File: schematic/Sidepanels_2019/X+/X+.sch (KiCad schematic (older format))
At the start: 33 parts, among them J1 Conn_01x04, J2 Conn_01x02

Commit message: Flipped and added TrisolX cells
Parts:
- added D16: D_Schottky, CySat footprints:Toshiba_CUS08F30, symbol Device:D_Schottky
- added SC17: Solar_Cell, CySat footprints:TriSelectSolarPanel_Left_Handed, symbol Device:Solar_Cell
- SC10, SC11, SC12, SC13, SC14, SC15, SC16, SC5, SC6, SC7, SC8, SC9: footprint CySat footprints:TriSelectSolarPanel -> CySat footprints:TriSelectSolarPanel_Left_Handed
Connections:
- net VCC: now also D16.1 (K), SC17.1 (+)
- net VSS: now also D16.2 (A), SC17.2 (-)
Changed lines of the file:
@@
 EESchema Schematic File Version 4
+LIBS:X+-cache
 EELAYER 29 0
 EELAYER END
@@
 F 0 "SC10" H 6308 2446 50  0000 L CNN
 F 1 "Solar_Cell" H 6308 2355 50  0000 L CNN
-F 2 "CySat footprints:TriSelectSolarPanel" V 6200 2410 50  0001 C CNN
+F 2 "CySat footprints:TriSelectSolarPanel_Left_Handed" V 6200 2410 50  0001 C CNN
 F 3 "~" V 6200 2410 50  0001 C CNN
 	1    6200 2350
@@
 F 0 "SC9" H 5458 2446 50  0000 L CNN
 F 1 "Solar_Cell" H 5458 2355 50  0000 L CNN
-F 2 "CySat footprints:TriSelectSolarPanel" V 5350 2410 50  0001 C CNN
+F 2 "CySat footprints:TriSelectSolarPanel_Left_Handed" V 5350 2410 50  0001 C CNN
 F 3 "~" V 5350 2410 50  0001 C CNN
 	1    5350 2350
@@
 F 0 "SC12" H 8008 2446 50  0000 L CNN
 F 1 "Solar_Cell" H 8008 2355 50  0000 L CNN
-F 2 "CySat footprints:TriSelectSolarPanel" V 7900 2410 50  0001 C CNN
+F 2 "CySat footprints:TriSelectSolarPanel_Left_Handed" V 7900 2410 50  0001 C CNN
 F 3 "~" V 7900 2410 50  0001 C CNN
 	1    7900 2350
@@
 F 0 "SC13" H 8708 2446 50  0000 L CNN
 F 1 "Solar_Cell" H 8708 2355 50  0000 L CNN
-F 2 "CySat footprints:TriSelectSolarPanel" V 8600 2410 50  0001 C CNN
+F 2 "CySat footprints:TriSelectSolarPanel_Left_Handed" V 8600 2410 50  0001 C CNN
 F 3 "~" V 8600 2410 50  0001 C CNN
 	1    8600 2350
@@
 F 0 "SC16" H 10808 2446 50  0000 L CNN
 F 1 "Solar_Cell" H 10808 2355 50  0000 L CNN
-F 2 "CySat footprints:TriSelectSolarPanel" V 10700 2410 50  0001 C CNN
+F 2 "CySat footprints:TriSelectSolarPanel_Left_Handed" V 10700 2410 50  0001 C CNN
 F 3 "~" V 10700 2410 50  0001 C CNN
 	1    10700 2350
@@
 F 0 "SC6" H 3108 2446 50  0000 L CNN
 F 1 "Solar_Cell" H 3108 2355 50  0000 L CNN
-F 2 "CySat footprints:TriSelectSolarPanel" V 3000 2410 50  0001 C CNN
+F 2 "CySat footprints:TriSelectSolarPanel_Left_Handed" V 3000 2410 50  0001 C CNN
 F 3 "~" V 3000 2410 50  0001 C CNN
 	1    3000 2350
@@
 F 0 "SC5" H 2458 2446 50  0000 L CNN
 F 1 "Solar_Cell" H 2458 2355 50  0000 L CNN
-F 2 "CySat footprints:TriSelectSolarPanel" V 2350 2410 50  0001 C CNN
+F 2 "CySat footprints:TriSelectSolarPanel_Left_Handed" V 2350 2410 50  0001 C CNN
 F 3 "~" V 2350 2410 50  0001 C CNN
 	1    2350 2350
@@
 F 0 "SC7" H 3758 2446 50  0000 L CNN
 F 1 "Solar_Cell" H 3758 2355 50  0000 L CNN
-F 2 "CySat footprints:TriSelectSolarPanel" V 3650 2410 50  0001 C CNN
+F 2 "CySat footprints:TriSelectSolarPanel_Left_Handed" V 3650 2410 50  0001 C CNN
 F 3 "~" V 3650 2410 50  0001 C CNN
 	1    3650 2350
@@
 F 0 "SC8" H 4608 2446 50  0000 L CNN
 F 1 "Solar_Cell" H 4608 2355 50  0000 L CNN
-F 2 "CySat footprints:TriSelectSolarPanel" V 4500 2410 50  0001 C CNN
+F 2 "CySat footprints:TriSelectSolarPanel_Left_Handed" V 4500 2410 50  0001 C CNN
 F 3 "~" V 4500 2410 50  0001 C CNN
 	1    4500 2350
@@
 F 0 "SC11" H 7158 2446 50  0000 L CNN
 F 1 "Solar_Cell" H 7158 2355 50  0000 L CNN
-F 2 "CySat footprints:TriSelectSolarPanel" V 7050 2410 50  0001 C CNN
+F 2 "CySat footprints:TriSelectSolarPanel_Left_Handed" V 7050 2410 50  0001 C CNN
 F 3 "~" V 7050 2410 50  0001 C CNN
 	1    7050 2350
@@
 F 0 "SC15" H 10108 2446 50  0000 L CNN
 F 1 "Solar_Cell" H 10108 2355 50  0000 L CNN
-F 2 "CySat footprints:TriSelectSolarPanel" V 10000 2410 50  0001 C CNN
+F 2 "CySat footprints:TriSelectSolarPanel_Left_Handed" V 10000 2410 50  0001 C CNN
 F 3 "~" V 10000 2410 50  0001 C CNN
 	1    10000 2350
@@
 F 0 "SC14" H 9408 2446 50  0000 L CNN
 F 1 "Solar_Cell" H 9408 2355 50  0000 L CNN
-F 2 "CySat footprints:TriSelectSolarPanel" V 9300 2410 50  0001 C CNN
+F 2 "CySat footprints:TriSelectSolarPanel_Left_Handed" V 9300 2410 50  0001 C CNN
 F 3 "~" V 9300 2410 50  0001 C CNN
 	1    9300 2350
@@
 Wire Wire Line
 	4800 1550 4200 1550
+$Comp
+L Device:Solar_Cell SC17
+U 1 1 5D90DC3A
+P 9700 2750
+F 0 "SC17" H 9808 2846 50  0000 L CNN
+F 1 "Solar_Cell" H 9808 2755 50  0000 L CNN
+F 2 "CySat footprints:TriSelectSolarPanel_Left_Handed" V 9700 2810 50  0001 C CNN
+F 3 "~" V 9700 2810 50  0001 C CNN
+	1    9700 2750
+	-1   0    0    1
+$EndComp
+$Comp
+L Device:D_Schottky D16
+U 1 1 5D90DC44
+P 10000 2800
+F 0 "D16" V 9954 2879 50  0000 L CNN
+F 1 "D_Schottky" V 10045 2879 50  0000 L CNN
+F 2 "CySat footprints:Toshiba_CUS08F30" H 10000 2800 50  0001 C CNN
+F 3 "~" H 10000 2800 50  0001 C CNN
+	1    10000 2800
+	0    -1   -1   0
+$EndComp
+Wire Wire Line
+	10000 2950 9850 2950
+Wire Wire Line
+	9700 2650 9850 2650
+Wire Wire Line
+	9850 3000 9850 2950
+Connection ~ 9850 2950
+Wire Wire Line
+	9850 2950 9700 2950
+Wire Wire Line
+	9850 2650 9850 2600
+Connection ~ 9850 2650
+Wire Wire Line
+	9850 2650 10000 2650
+Wire Wire Line
+	10650 2600 10650 2500
+Wire Wire Line
+	10650 2500 10550 2500
+Wire Wire Line
+	9850 2600 10650 2600
+Connection ~ 10550 2500
+Wire Wire Line
+	10900 3000 10900 2100
+Wire Wire Line
+	10900 2100 10550 2100
+Wire Wire Line
+	9850 3000 10900 3000
+Connection ~ 10550 2100
 $EndSCHEMATC

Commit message: Flipped/removed Trisol Cells
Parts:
- removed D16: D_Schottky, CySat footprints:Toshiba_CUS08F30, symbol Device:D_Schottky
- removed SC17: Solar_Cell, CySat footprints:TriSelectSolarPanel_Left_Handed, symbol Device:Solar_Cell
- SC10, SC11, SC12, SC13, SC14, SC15, SC16, SC7, SC8, SC9: footprint CySat footprints:TriSelectSolarPanel_Left_Handed -> CySat footprints:TriSelectSolarPanel
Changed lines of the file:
@@
 F 0 "SC10" H 6308 2446 50  0000 L CNN
 F 1 "Solar_Cell" H 6308 2355 50  0000 L CNN
-F 2 "CySat footprints:TriSelectSolarPanel_Left_Handed" V 6200 2410 50  0001 C CNN
+F 2 "CySat footprints:TriSelectSolarPanel" V 6200 2410 50  0001 C CNN
 F 3 "~" V 6200 2410 50  0001 C CNN
 	1    6200 2350
@@
 F 0 "SC9" H 5458 2446 50  0000 L CNN
 F 1 "Solar_Cell" H 5458 2355 50  0000 L CNN
-F 2 "CySat footprints:TriSelectSolarPanel_Left_Handed" V 5350 2410 50  0001 C CNN
+F 2 "CySat footprints:TriSelectSolarPanel" V 5350 2410 50  0001 C CNN
 F 3 "~" V 5350 2410 50  0001 C CNN
 	1    5350 2350
@@
 F 0 "SC12" H 8008 2446 50  0000 L CNN
 F 1 "Solar_Cell" H 8008 2355 50  0000 L CNN
-F 2 "CySat footprints:TriSelectSolarPanel_Left_Handed" V 7900 2410 50  0001 C CNN
+F 2 "CySat footprints:TriSelectSolarPanel" V 7900 2410 50  0001 C CNN
 F 3 "~" V 7900 2410 50  0001 C CNN
 	1    7900 2350
@@
 F 0 "SC13" H 8708 2446 50  0000 L CNN
 F 1 "Solar_Cell" H 8708 2355 50  0000 L CNN
-F 2 "CySat footprints:TriSelectSolarPanel_Left_Handed" V 8600 2410 50  0001 C CNN
+F 2 "CySat footprints:TriSelectSolarPanel" V 8600 2410 50  0001 C CNN
 F 3 "~" V 8600 2410 50  0001 C CNN
 	1    8600 2350
@@
 F 0 "SC16" H 10808 2446 50  0000 L CNN
 F 1 "Solar_Cell" H 10808 2355 50  0000 L CNN
-F 2 "CySat footprints:TriSelectSolarPanel_Left_Handed" V 10700 2410 50  0001 C CNN
+F 2 "CySat footprints:TriSelectSolarPanel" V 10700 2410 50  0001 C CNN
 F 3 "~" V 10700 2410 50  0001 C CNN
 	1    10700 2350
@@
 F 0 "SC7" H 3758 2446 50  0000 L CNN
 F 1 "Solar_Cell" H 3758 2355 50  0000 L CNN
-F 2 "CySat footprints:TriSelectSolarPanel_Left_Handed" V 3650 2410 50  0001 C CNN
+F 2 "CySat footprints:TriSelectSolarPanel" V 3650 2410 50  0001 C CNN
 F 3 "~" V 3650 2410 50  0001 C CNN
 	1    3650 2350
@@
 F 0 "SC8" H 4608 2446 50  0000 L CNN
 F 1 "Solar_Cell" H 4608 2355 50  0000 L CNN
-F 2 "CySat footprints:TriSelectSolarPanel_Left_Handed" V 4500 2410 50  0001 C CNN
+F 2 "CySat footprints:TriSelectSolarPanel" V 4500 2410 50  0001 C CNN
 F 3 "~" V 4500 2410 50  0001 C CNN
 	1    4500 2350
@@
 F 0 "SC11" H 7158 2446 50  0000 L CNN
 F 1 "Solar_Cell" H 7158 2355 50  0000 L CNN
-F 2 "CySat footprints:TriSelectSolarPanel_Left_Handed" V 7050 2410 50  0001 C CNN
+F 2 "CySat footprints:TriSelectSolarPanel" V 7050 2410 50  0001 C CNN
 F 3 "~" V 7050 2410 50  0001 C CNN
 	1    7050 2350
@@
 F 0 "SC15" H 10108 2446 50  0000 L CNN
 F 1 "Solar_Cell" H 10108 2355 50  0000 L CNN
-F 2 "CySat footprints:TriSelectSolarPanel_Left_Handed" V 10000 2410 50  0001 C CNN
+F 2 "CySat footprints:TriSelectSolarPanel" V 10000 2410 50  0001 C CNN
 F 3 "~" V 10000 2410 50  0001 C CNN
 	1    10000 2350
@@
 F 0 "SC14" H 9408 2446 50  0000 L CNN
 F 1 "Solar_Cell" H 9408 2355 50  0000 L CNN
-F 2 "CySat footprints:TriSelectSolarPanel_Left_Handed" V 9300 2410 50  0001 C CNN
+F 2 "CySat footprints:TriSelectSolarPanel" V 9300 2410 50  0001 C CNN
 F 3 "~" V 9300 2410 50  0001 C CNN
 	1    9300 2350
@@
 Wire Wire Line
 	4800 1550 4200 1550
-$Comp
-L Device:Solar_Cell SC17
-U 1 1 5D90DC3A
-P 9700 2750
-F 0 "SC17" H 9808 2846 50  0000 L CNN
-F 1 "Solar_Cell" H 9808 2755 50  0000 L CNN
-F 2 "CySat footprints:TriSelectSolarPanel_Left_Handed" V 9700 2810 50  0001 C CNN
-F 3 "~" V 9700 2810 50  0001 C CNN
-	1    9700 2750
-	-1   0    0    1
-$EndComp
-$Comp
-L Device:D_Schottky D16
-U 1 1 5D90DC44
-P 10000 2800
-F 0 "D16" V 9954 2879 50  0000 L CNN
-F 1 "D_Schottky" V 10045 2879 50  0000 L CNN
-F 2 "CySat footprints:Toshiba_CUS08F30" H 10000 2800 50  0001 C CNN
-F 3 "~" H 10000 2800 50  0001 C CNN
-	1    10000 2800
-	0    -1   -1   0
-$EndComp
-Wire Wire Line
-	10000 2950 9850 2950
-Wire Wire Line
-	9700 2650 9850 2650
-Wire Wire Line
-	9850 3000 9850 2950
-Connection ~ 9850 2950
-Wire Wire Line
-	9850 2950 9700 2950
-Wire Wire Line
-	9850 2650 9850 2600
-Connection ~ 9850 2650
-Wire Wire Line
-	9850 2650 10000 2650
-Wire Wire Line
-	10650 2600 10650 2500
-Wire Wire Line
-	10650 2500 10550 2500
-Wire Wire Line
-	9850 2600 10650 2600
-Connection ~ 10550 2500
-Wire Wire Line
-	10900 3000 10900 2100
-Wire Wire Line
-	10900 2100 10550 2100
-Wire Wire Line
-	9850 3000 10900 3000
-Connection ~ 10550 2100
 $EndSCHEMATC

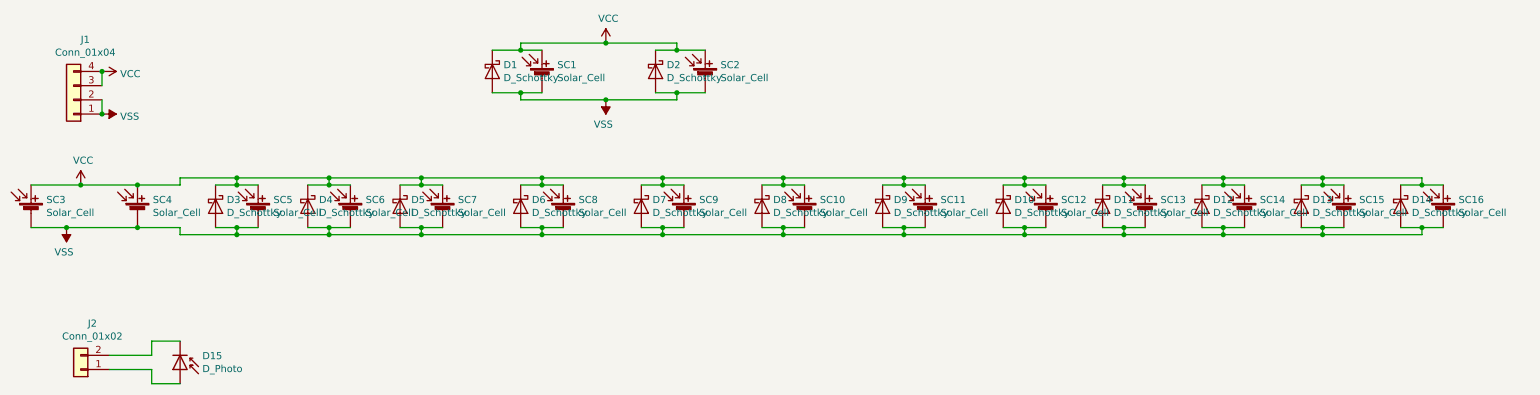
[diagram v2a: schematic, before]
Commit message: Update to X panels
Routing completed on both, solar panel change out complete on X+.  Re-did library and page settings.  DRC checks out.
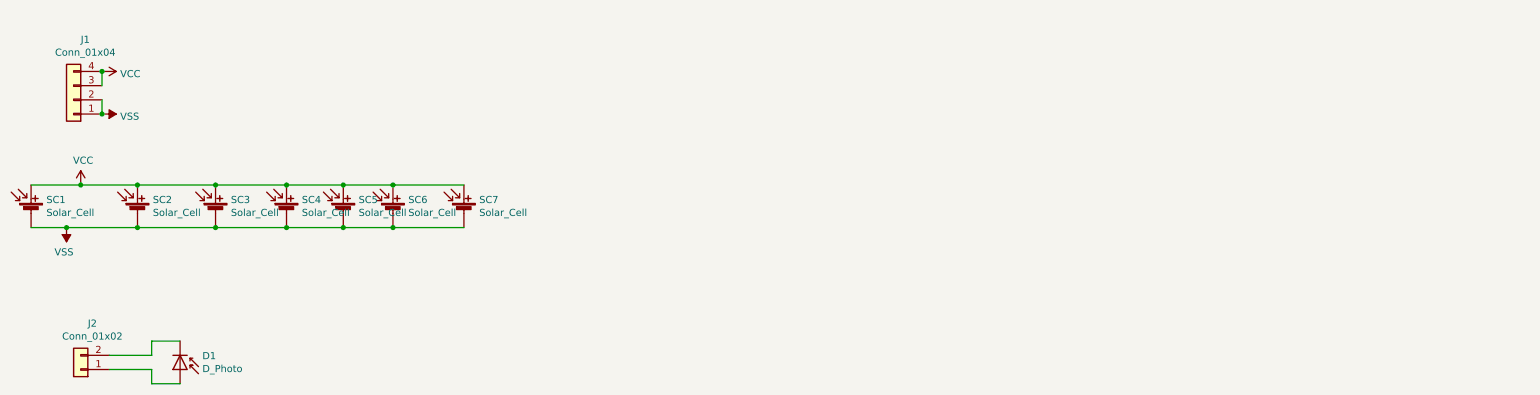
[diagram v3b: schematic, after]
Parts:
- removed D1, D10, D11, D12, D13, D14, D2, D3, D4, D5, D6, D7, D8, D9: D_Schottky, CySat footprints:Toshiba_CUS08F30, symbol Device:D_Schottky
- removed SC1, SC2: Solar_Cell, CySat footprints:ISS_SolarCell, symbol Device:Solar_Cell
- removed SC10, SC11, SC12, SC13, SC14, SC15, SC16, SC8, SC9: Solar_Cell, CySat footprints:TriSelectSolarPanel, symbol Device:Solar_Cell
- added SC3, SC4: Solar_Cell, CySat_Solar:Spectrolab, symbol Device:Solar_Cell
- D1: renamed from D15; footprint CySat footprints:Sun_Sensor -> Diode_SMD:D_0805_2012Metric
- SC1: renamed from SC3; footprint CySat footprints:Spectrolab -> CySat_Solar:Spectrolab
- SC2: renamed from SC4; footprint CySat footprints:Spectrolab -> CySat_Solar:Spectrolab
- SC5, SC6: footprint CySat footprints:TriSelectSolarPanel_Left_Handed -> CySat_Solar:Spectrolab
- SC7: footprint CySat footprints:TriSelectSolarPanel -> CySat_Solar:Spectrolab
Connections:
- net VCC: now also SC3.1 (+), SC4.1 (+)
- net VSS: now also SC3.2 (-), SC4.2 (-)
